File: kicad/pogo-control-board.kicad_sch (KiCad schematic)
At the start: 78 parts, among them CN1 CN_CTRL_1, CN2 CN_CTRL_2, CN3 CN_CTRL_3_PLACEHOLDER_TBD, J1 L IN, J10 BYPASS CV, J11 OFFSET CV, J12 BLEND CV, J13 FREQ CV1, J14 FB CV1, J15 DRIVE CV1, J16 FREQ CV2, J17 FB CV2, J18 DRIVE CV2, J19 FREQ CV3, J2 R IN, J20 FB CV3, J21 DRIVE CV3, J22 VCA CV IN, J23 LP1 CUT CV, J24 LP1 RES CV, J25 LP2 CUT CV, J26 LP2 RES CV, J27 HP CUT CV, J28 HP RES CV, J3 ENV L, J4 ENV R, J5 BAND OUT L, J6 BAND OUT R, J7 LEFT OUT, J8 RIGHT OUT, J9 MOD IN, SW1 GAIN 1x/5x, SW2 MOD SRC SEL, SW3 POLARITY, SW4 MODE

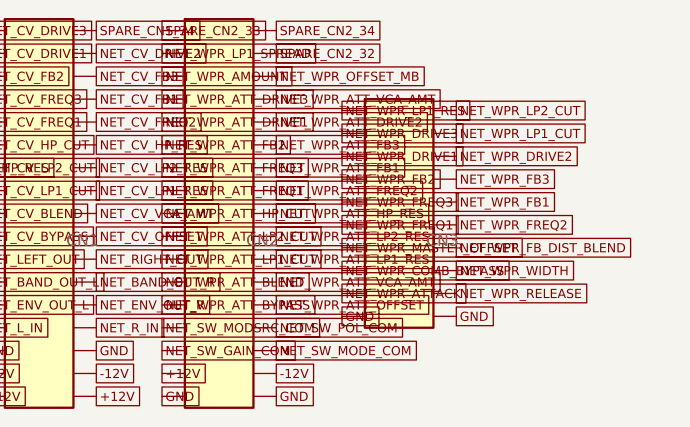
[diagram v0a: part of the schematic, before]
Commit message: Fix three net/connector bugs in KiCad control board generator
1. CN2 pin 28 duplicate: NET_WPR_ATT_VCA_AMT was assigned to both pin 12
   (attenuverter wiper, correct) and pin 28 (duplicate, wrong). Pin 28 is
   now SPARE_CN2_28. VCA AMT is destination #4 of 19 — it was already on pin 12.

2. CN3 overflow: extended from 20-pin to 24-pin (2×12). LP2_RES, HP_CUT, and
   HP_RES wipers were falling off the end of the 20-pin connector with only a
   comment. All 23 signals now fit with 1 spare.

3. MODE switch pins on CN2: pins 6–8 previously carried NET_SW_MODE_COM (the
   switch common — useless to the utility board). Now carry the 3 position
   outputs: NET_SW_MODE_SFT / _HRD / _WFD, which the utility board actually
   needs to decode CD4053 state. Added detailed comment on the 1-vs-3 switch
   ambiguity (panel-notes vs layout-notes conflict, unresolved, flagged).

Also updated kicad-process.md to reflect corrected CN3 size (24-pin), clarify
the layout-notes "19 + VCA AMT = 20" wording issue, and document MODE switch
encoding approach.

https://claude.ai/code/session_01JzWGptzLTqFkAZDHVU6Z8A
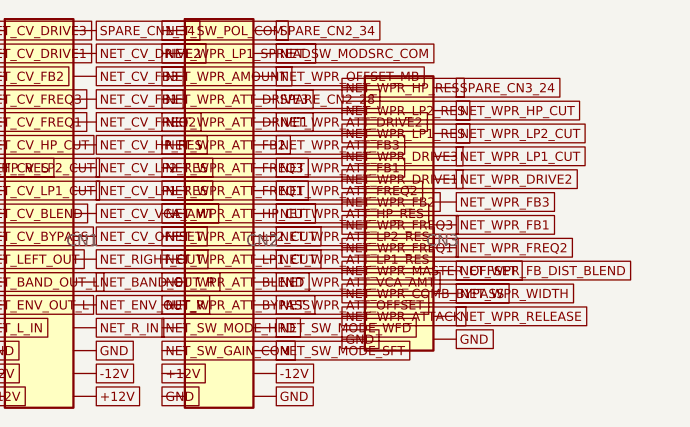
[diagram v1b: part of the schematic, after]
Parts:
- removed CN3: CN_CTRL_3_PLACEHOLDER_TBD, symbol Connector_IDC:IDC-Header_2x10_P2.54mm_Vertical
- added CN3: CN_CTRL_3_PLACEHOLDER_TBD, symbol Connector_IDC:IDC-Header_2x12_P2.54mm_Vertical
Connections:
- net SPARE_CN2_32 is gone; now on net NET_SW_MODSRC_COM: CN2.4 (Pin_4)
- net SPARE_CN2_33 is gone; now on net NET_SW_POL_COM: CN2.1 (Pin_1)
- net GND: now also CN3.23 (Pin_23), CN3.24 (Pin_24)
- net NET_SW_MODE_COM: no longer CN2.30 (Pin_30)
- net NET_SW_MODE_HRD: now also CN2.27 (Pin_27)
- net NET_SW_MODE_SFT: now also CN2.30 (Pin_30)
- net NET_SW_MODE_WFD: now also CN2.28 (Pin_28)
- net NET_SW_MODSRC_COM: no longer CN2.27 (Pin_27)
- net NET_SW_POL_COM: no longer CN2.28 (Pin_28)
- net NET_WPR_ATTACK: now also CN3.21 (Pin_21)
- net NET_WPR_ATT_VCA_AMT: no longer CN2.8 (Pin_8)
- net NET_WPR_COMB_BYPASS: now also CN3.19 (Pin_19)
- net NET_WPR_DRIVE1: now also CN3.9 (Pin_9)
- net NET_WPR_DRIVE2: now also CN3.10 (Pin_10)
- net NET_WPR_DRIVE3: now also CN3.7 (Pin_7)
- net NET_WPR_FB1: now also CN3.14 (Pin_14)
- net NET_WPR_FB2: now also CN3.11 (Pin_11)
- net NET_WPR_FB3: now also CN3.12 (Pin_12)
- net NET_WPR_FB_DIST_BLEND: now also CN3.18 (Pin_18)
- net NET_WPR_FREQ1: now also CN3.15 (Pin_15)
- net NET_WPR_FREQ2: now also CN3.16 (Pin_16)
- net NET_WPR_FREQ3: now also CN3.13 (Pin_13)
- net NET_WPR_HP_CUT: now also CN3.4 (Pin_4)
- net NET_WPR_HP_RES: now also CN3.1 (Pin_1)
- net NET_WPR_LP1_CUT: now also CN3.8 (Pin_8)
- net NET_WPR_LP1_RES: now also CN3.5 (Pin_5)
- net NET_WPR_LP2_CUT: now also CN3.6 (Pin_6)
- net NET_WPR_LP2_RES: now also CN3.3 (Pin_3)
- net NET_WPR_MASTER_OFFSET: now also CN3.17 (Pin_17)
- net NET_WPR_RELEASE: now also CN3.22 (Pin_22)
- net NET_WPR_WIDTH: now also CN3.20 (Pin_20)
- new net SPARE_CN2_28: CN2.8 (Pin_8)
- new net SPARE_CN3_24: CN3.2 (Pin_2)

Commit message: Fix control board schematic: expand CN2 to 40-pin, wire all switch nets
All switch commons now tie to +12V power symbols on the control board
(no orphan global labels). SP3T position outputs (MODE, MOD SRC, POLARITY)
each get 3 individual connector pins instead of sending the common pin:

CN_CTRL_2 expanded from 34-pin to 40-pin (2×20):
- Pins 32–34: MOD SRC L/MAX/AVG position outputs (SW2)
- Pins 35–37: POLARITY POS/OFF/NEG position outputs (SW3)
- Pin 38: ENV NORM return (utility board → MOD IN jack SW lug for normalling)

CN_CTRL_1 pin 34 changed from SPARE to NET_MOD_IN (MOD IN jack tip).

Result: zero problematic floating nets. Remaining 23 single-occurrence
nets are all intentional: 19 NET_MODBUS_NORM_* (CV override normalling,
documented in kicad-process.md), 4 SPARE_* connector spare pins.

Updated layout-notes.md and kicad-process.md to match.

https://claude.ai/code/session_01JzWGptzLTqFkAZDHVU6Z8A
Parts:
- removed CN2: CN_CTRL_2, symbol Connector_IDC:IDC-Header_2x17_P2.54mm_Vertical
- added CN2: CN_CTRL_2, symbol Connector_IDC:IDC-Header_2x20_P2.54mm_Vertical
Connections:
- net NET_SW_GAIN_1X is gone; now on net GND: SW1.2 (B)
- net NET_SW_GAIN_5X is gone; now on net +12V: SW1.1 (A)
- net NET_SW_MODE_COM is gone; now on net +12V: SW4.4 (C)
- net NET_SW_MODSRC_COM is gone; now on net +12V: SW2.4 (C)
- net NET_SW_POL_COM is gone; now on net +12V: SW3.4 (C)
- net SPARE_CN1_34 is gone; now on net NET_MOD_IN: CN1.2 (Pin_2)
- net +12V: now also CN2.37 (Pin_37)
- net -12V: now also CN2.38 (Pin_38)
- net GND: now also CN2.39 (Pin_39), CN2.40 (Pin_40)
- net NET_ENV_NORM: now also CN2.4 (Pin_4)
- net NET_SW_GAIN_COM: now also CN2.35 (Pin_35)
- net NET_SW_MODE_HRD: now also CN2.33 (Pin_33)
- net NET_SW_MODE_SFT: now also CN2.36 (Pin_36)
- net NET_SW_MODE_WFD: now also CN2.34 (Pin_34)
- net NET_SW_MODSRC_AVG: now also CN2.8 (Pin_8)
- net NET_SW_MODSRC_L: now also CN2.10 (Pin_10)
- net NET_SW_MODSRC_MAX: now also CN2.7 (Pin_7)
- net NET_SW_POL_NEG: now also CN2.3 (Pin_3)
- net NET_SW_POL_OFF: now also CN2.6 (Pin_6)
- net NET_SW_POL_POS: now also CN2.5 (Pin_5)
- net NET_WPR_AMOUNT: now also CN2.11 (Pin_11)
- net NET_WPR_ATT_BLEND: now also CN2.29 (Pin_29)
- net NET_WPR_ATT_BYPASS: now also CN2.31 (Pin_31)
- net NET_WPR_ATT_DRIVE1: now also CN2.15 (Pin_15)
- net NET_WPR_ATT_DRIVE2: now also CN2.16 (Pin_16)
- net NET_WPR_ATT_DRIVE3: now also CN2.13 (Pin_13)
- net NET_WPR_ATT_FB1: now also CN2.20 (Pin_20)
- net NET_WPR_ATT_FB2: now also CN2.17 (Pin_17)
- net NET_WPR_ATT_FB3: now also CN2.18 (Pin_18)
- net NET_WPR_ATT_FREQ1: now also CN2.21 (Pin_21)
- net NET_WPR_ATT_FREQ2: now also CN2.22 (Pin_22)
- net NET_WPR_ATT_FREQ3: now also CN2.19 (Pin_19)
- net NET_WPR_ATT_HP_CUT: now also CN2.23 (Pin_23)
- net NET_WPR_ATT_HP_RES: now also CN2.24 (Pin_24)
- net NET_WPR_ATT_LP1_CUT: now also CN2.27 (Pin_27)
- net NET_WPR_ATT_LP1_RES: now also CN2.28 (Pin_28)
- net NET_WPR_ATT_LP2_CUT: now also CN2.25 (Pin_25)
- net NET_WPR_ATT_LP2_RES: now also CN2.26 (Pin_26)
- net NET_WPR_ATT_OFFSET: now also CN2.32 (Pin_32)
- net NET_WPR_ATT_VCA_AMT: now also CN2.30 (Pin_30)
- net NET_WPR_LP1_SPREAD: now also CN2.9 (Pin_9)
- net NET_WPR_OFFSET_MB: now also CN2.12 (Pin_12)
- net SPARE_CN2_28: now also CN2.14 (Pin_14)
- new net SPARE_CN2_39: CN2.1 (Pin_1)
- new net SPARE_CN2_40: CN2.2 (Pin_2)
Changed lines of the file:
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@@
     (effects (font (size 1.016 1.016)) (justify left) (hide yes)))
 )
-(global_label "NET_SW_GAIN_1X"
-  (shape passive)
+(global_label "NET_SW_GAIN_COM"
+  (shape passive)
+  (at 63.810 50.000 0)
+  (effects (font (size 1.016 1.016)) (justify left))
+)
+(symbol
+  (lib_id "power:GND")
   (at 56.190 52.032 0)
-  (effects (font (size 1.016 1.016)) (justify left))
-)
-(global_label "NET_SW_GAIN_5X"
-  (shape passive)
+  (unit 1) (in_bom yes) (on_board yes)
+  (property "Reference" "#PWR" (at 56.190 50.032 0)
+    (effects (font (size 1.016 1.016)) (hide yes)))
+  (property "Value" "GND" (at 56.190 54.032 0)
+    (effects (font (size 1.016 1.016))))
+)
+(symbol
+  (lib_id "power:+12V")
   (at 56.190 47.968 0)
-  (effects (font (size 1.016 1.016)) (justify left))
-)
-(global_label "NET_SW_GAIN_COM"
-  (shape passive)
-  (at 63.810 50.000 0)
-  (effects (font (size 1.016 1.016)) (justify left))
+  (unit 1) (in_bom yes) (on_board yes)
+  (property "Reference" "#PWR" (at 56.190 45.968 0)
+    (effects (font (size 1.016 1.016)) (hide yes)))
+  (property "Value" "+12V" (at 56.190 49.968 0)
+    (effects (font (size 1.016 1.016))))
 )
 (symbol
@@
   (effects (font (size 1.016 1.016)) (justify left))
 )
-(global_label "NET_SW_MODSRC_COM"
-  (shape passive)
+(symbol
+  (lib_id "power:+12V")
   (at 83.810 50.000 0)
-  (effects (font (size 1.016 1.016)) (justify left))
+  (unit 1) (in_bom yes) (on_board yes)
+  (property "Reference" "#PWR" (at 83.810 48.000 0)
+    (effects (font (size 1.016 1.016)) (hide yes)))
+  (property "Value" "+12V" (at 83.810 52.000 0)
+    (effects (font (size 1.016 1.016))))
 )
 (symbol
@@
   (effects (font (size 1.016 1.016)) (justify left))
 )
-(global_label "NET_SW_POL_COM"
-  (shape passive)
+(symbol
+  (lib_id "power:+12V")
   (at 283.810 50.000 0)
-  (effects (font (size 1.016 1.016)) (justify left))
+  (unit 1) (in_bom yes) (on_board yes)
+  (property "Reference" "#PWR" (at 283.810 48.000 0)
+    (effects (font (size 1.016 1.016)) (hide yes)))
+  (property "Value" "+12V" (at 283.810 52.000 0)
+    (effects (font (size 1.016 1.016))))
 )
 (symbol
@@
   (effects (font (size 1.016 1.016)) (justify left))
 )
-(global_label "NET_SW_MODE_COM"
-  (shape passive)
+(symbol
+  (lib_id "power:+12V")
   (at 323.810 50.000 0)
-  (effects (font (size 1.016 1.016)) (justify left))
+  (unit 1) (in_bom yes) (on_board yes)
+  (property "Reference" "#PWR" (at 323.810 48.000 0)
+    (effects (font (size 1.016 1.016)) (hide yes)))
+  (property "Value" "+12V" (at 323.810 52.000 0)
+    (effects (font (size 1.016 1.016))))
 )
 (symbol
@@
   (effects (font (size 1.016 1.016)) (justify left))
 )
-(global_label "SPARE_CN1_34"
+(global_label "NET_MOD_IN"
   (shape passive)
   (at 1526.350 29.680 0)
@@
 )
 (symbol
-  (lib_id "Connector_IDC:IDC-Header_2x17_P2.54mm_Vertical")
+  (lib_id "Connector_IDC:IDC-Header_2x20_P2.54mm_Vertical")
   (at 1540.000 50.000 0)
   (unit 1)
@@
 (global_label "GND"
   (shape passive)
-  (at 1533.650 70.320 0)
-  (effects (font (size 1.016 1.016)) (justify left))
-)
-(global_label "GND"
-  (shape passive)
-  (at 1546.350 70.320 0)
-  (effects (font (size 1.016 1.016)) (justify left))
-)
-(global_label "+12V"
-  (shape passive)
-  (at 1533.650 67.780 0)
-  (effects (font (size 1.016 1.016)) (justify left))
-)
-(global_label "-12V"
-  (shape passive)
-  (at 1546.350 67.780 0)
+  (at 1533.650 74.130 0)
+  (effects (font (size 1.016 1.016)) (justify left))
+)
+(global_label "GND"
+  (shape passive)
+  (at 1546.350 74.130 0)
+  (effects (font (size 1.016 1.016)) (justify left))
+)
+(global_label "+12V"
+  (shape passive)
+  (at 1533.650 71.590 0)
+  (effects (font (size 1.016 1.016)) (justify left))
+)
+(global_label "-12V"
+  (shape passive)
+  (at 1546.350 71.590 0)
   (effects (font (size 1.016 1.016)) (justify left))
 )
 (global_label "NET_SW_GAIN_COM"
   (shape passive)
-  (at 1533.650 65.240 0)
+  (at 1533.650 69.050 0)
   (effects (font (size 1.016 1.016)) (justify left))
 )
 (global_label "NET_SW_MODE_SFT"
   (shape passive)
-  (at 1546.350 65.240 0)
+  (at 1546.350 69.050 0)
   (effects (font (size 1.016 1.016)) (justify left))
 )
 (global_label "NET_SW_MODE_HRD"
   (shape passive)
-  (at 1533.650 62.700 0)
+  (at 1533.650 66.510 0)
   (effects (font (size 1.016 1.016)) (justify left))
 )
 (global_label "NET_SW_MODE_WFD"
   (shape passive)
-  (at 1546.350 62.700 0)
+  (at 1546.350 66.510 0)
   (effects (font (size 1.016 1.016)) (justify left))
 )
 (global_label "NET_WPR_ATT_BYPASS"
   (shape passive)
-  (at 1533.650 60.160 0)
+  (at 1533.650 63.970 0)
   (effects (font (size 1.016 1.016)) (justify left))
 )
 (global_label "NET_WPR_ATT_OFFSET"
   (shape passive)
-  (at 1546.350 60.160 0)
+  (at 1546.350 63.970 0)
   (effects (font (size 1.016 1.016)) (justify left))
 )
 (global_label "NET_WPR_ATT_BLEND"
   (shape passive)
-  (at 1533.650 57.620 0)
+  (at 1533.650 61.430 0)
   (effects (font (size 1.016 1.016)) (justify left))
 )
 (global_label "NET_WPR_ATT_VCA_AMT"
   (shape passive)
-  (at 1546.350 57.620 0)
+  (at 1546.350 61.430 0)
   (effects (font (size 1.016 1.016)) (justify left))
 )
 (global_label "NET_WPR_ATT_LP1_CUT"
   (shape passive)
-  (at 1533.650 55.080 0)
+  (at 1533.650 58.890 0)
   (effects (font (size 1.016 1.016)) (justify left))
 )
 (global_label "NET_WPR_ATT_LP1_RES"
   (shape passive)
-  (at 1546.350 55.080 0)
+  (at 1546.350 58.890 0)
   (effects (font (size 1.016 1.016)) (justify left))
 )
 (global_label "NET_WPR_ATT_LP2_CUT"
   (shape passive)
-  (at 1533.650 52.540 0)
+  (at 1533.650 56.350 0)
   (effects (font (size 1.016 1.016)) (justify left))
 )
 (global_label "NET_WPR_ATT_LP2_RES"
   (shape passive)
-  (at 1546.350 52.540 0)
+  (at 1546.350 56.350 0)
   (effects (font (size 1.016 1.016)) (justify left))
 )
 (global_label "NET_WPR_ATT_HP_CUT"
   (shape passive)
-  (at 1533.650 50.000 0)
+  (at 1533.650 53.810 0)
   (effects (font (size 1.016 1.016)) (justify left))
 )
 (global_label "NET_WPR_ATT_HP_RES"
   (shape passive)
-  (at 1546.350 50.000 0)
+  (at 1546.350 53.810 0)
   (effects (font (size 1.016 1.016)) (justify left))
 )
 (global_label "NET_WPR_ATT_FREQ1"
   (shape passive)
-  (at 1533.650 47.460 0)
+  (at 1533.650 51.270 0)
   (effects (font (size 1.016 1.016)) (justify left))
 )
 (global_label "NET_WPR_ATT_FREQ2"
   (shape passive)
-  (at 1546.350 47.460 0)
+  (at 1546.350 51.270 0)
   (effects (font (size 1.016 1.016)) (justify left))
 )
 (global_label "NET_WPR_ATT_FREQ3"
   (shape passive)
-  (at 1533.650 44.920 0)
+  (at 1533.650 48.730 0)
   (effects (font (size 1.016 1.016)) (justify left))
 )
 (global_label "NET_WPR_ATT_FB1"
   (shape passive)
-  (at 1546.350 44.920 0)
+  (at 1546.350 48.730 0)
   (effects (font (size 1.016 1.016)) (justify left))
 )
 (global_label "NET_WPR_ATT_FB2"
   (shape passive)
-  (at 1533.650 42.380 0)
+  (at 1533.650 46.190 0)
   (effects (font (size 1.016 1.016)) (justify left))
 )
 (global_label "NET_WPR_ATT_FB3"
   (shape passive)
-  (at 1546.350 42.380 0)
+  (at 1546.350 46.190 0)
   (effects (font (size 1.016 1.016)) (justify left))
 )
 (global_label "NET_WPR_ATT_DRIVE1"
   (shape passive)
-  (at 1533.650 39.840 0)
+  (at 1533.650 43.650 0)
   (effects (font (size 1.016 1.016)) (justify left))
 )
 (global_label "NET_WPR_ATT_DRIVE2"
   (shape passive)
-  (at 1546.350 39.840 0)
+  (at 1546.350 43.650 0)
   (effects (font (size 1.016 1.016)) (justify left))
 )
 (global_label "NET_WPR_ATT_DRIVE3"
   (shape passive)
-  (at 1533.650 37.300 0)
+  (at 1533.650 41.110 0)
   (effects (font (size 1.016 1.016)) (justify left))
 )
 (global_label "SPARE_CN2_28"
   (shape passive)
-  (at 1546.350 37.300 0)
+  (at 1546.350 41.110 0)
   (effects (font (size 1.016 1.016)) (justify left))
 )
 (global_label "NET_WPR_AMOUNT"
   (shape passive)
-  (at 1533.650 34.760 0)
+  (at 1533.650 38.570 0)
   (effects (font (size 1.016 1.016)) (justify left))
 )
 (global_label "NET_WPR_OFFSET_MB"
   (shape passive)
-  (at 1546.350 34.760 0)
+  (at 1546.350 38.570 0)
   (effects (font (size 1.016 1.016)) (justify left))
 )
 (global_label "NET_WPR_LP1_SPREAD"
   (shape passive)
-  (at 1533.650 32.220 0)
-  (effects (font (size 1.016 1.016)) (justify left))
-)
-(global_label "NET_SW_MODSRC_COM"
-  (shape passive)
-  (at 1546.350 32.220 0)
-  (effects (font (size 1.016 1.016)) (justify left))
-)
-(global_label "NET_SW_POL_COM"
-  (shape passive)
-  (at 1533.650 29.680 0)
-  (effects (font (size 1.016 1.016)) (justify left))
-)
-(global_label "SPARE_CN2_34"
-  (shape passive)
-  (at 1546.350 29.680 0)
-  (effects (font (size 1.016 1.016)) (justify left))
-)
+  (at 1533.650 36.030 0)
+  (effects (font (size 1.016 1.016)) (justify left))
+)
+(global_label "NET_SW_MODSRC_L"
+  (shape passive)
+  (at 1546.350 36.030 0)
+  (effects (font (size 1.016 1.016)) (justify left))
+)
+(global_label "NET_SW_MODSRC_MAX"
+  (shape passive)
+  (at 1533.650 33.490 0)
+  (effects (font (size 1.016 1.016)) (justify left))
+)
+(global_label "NET_SW_MODSRC_AVG"
+  (shape passive)
+  (at 1546.350 33.490 0)
+  (effects (font (size 1.016 1.016)) (justify left))
+)
+(global_label "NET_SW_POL_POS"
+  (shape passive)
+  (at 1533.650 30.950 0)
+  (effects (font (size 1.016 1.016)) (justify left))
+)
+(global_label "NET_SW_POL_OFF"
+  (shape passive)
+  (at 1546.350 30.950 0)
+  (effects (font (size 1.016 1.016)) (justify left))
+)
+(global_label "NET_SW_POL_NEG"
+  (shape passive)
+  (at 1533.650 28.410 0)
+  (effects (font (size 1.016 1.016)) (justify left))
+)
+(global_label "NET_ENV_NORM"
+  (shape passive)
+  (at 1546.350 28.410 0)
+  (effects (font (size 1.016 1.016)) (justify left))
+)
+(global_label "SPARE_CN2_39"
+  (shape passive)
+  (at 1533.650 25.870 0)
+  (effects (font (size 1.016 1.016)) (justify left))
+)
+(global_label "SPARE_CN2_40"
+  (shape passive)
+  (at 1546.350 25.870 0)
+  (effects (font (size 1.016 1.016)) (justify left))
+)

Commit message: Collapse 19 MODBUS_NORM_* nets into single NET_MODBUS_NORM (1 connector pin)
All 19 CV override jack SW lugs now share one net (NET_MODBUS_NORM) wired
together on the control board PCB. The utility board drives CN_CTRL_2 pin 39
with the processed Mod Bus output (post-AMOUNT/OFFSET, buffered). When no
cable is plugged into any CV override jack, its Thonkiconn switch connects
tip to SW, so the attenuverter input sees the Mod Bus.

This saves 18 connector pins vs. individual normalling signals and eliminates
all 19 previously-floating NET_MODBUS_NORM_* labels.

Result: only 3 single-occurrence nets remain — all are intentional spare pins
(SPARE_CN2_28, SPARE_CN2_40, SPARE_CN3_24).

Updated layout-notes.md and kicad-process.md to document the design.

https://claude.ai/code/session_01JzWGptzLTqFkAZDHVU6Z8A
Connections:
- net SPARE_CN2_39 renamed NET_MODBUS_NORM
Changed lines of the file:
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@@
   (effects (font (size 1.016 1.016)) (justify left))
 )
-(global_label "NET_MODBUS_NORM_BYPASS"
+(global_label "NET_MODBUS_NORM"
   (shape passive)
   (at 360.000 44.920 0)
@@
   (effects (font (size 1.016 1.016)) (justify left))
 )
-(global_label "NET_MODBUS_NORM_OFFSET"
+(global_label "NET_MODBUS_NORM"
   (shape passive)
   (at 380.000 44.920 0)
@@
   (effects (font (size 1.016 1.016)) (justify left))
 )
-(global_label "NET_MODBUS_NORM_BLEND"
+(global_label "NET_MODBUS_NORM"
   (shape passive)
   (at 400.000 44.920 0)
@@
   (effects (font (size 1.016 1.016)) (justify left))
 )
-(global_label "NET_MODBUS_NORM_FREQ1"
+(global_label "NET_MODBUS_NORM"
   (shape passive)
   (at 600.000 44.920 0)
@@
   (effects (font (size 1.016 1.016)) (justify left))
 )
-(global_label "NET_MODBUS_NORM_FB1"
+(global_label "NET_MODBUS_NORM"
   (shape passive)
   (at 620.000 44.920 0)
@@
   (effects (font (size 1.016 1.016)) (justify left))
 )
-(global_label "NET_MODBUS_NORM_DRIVE1"
+(global_label "NET_MODBUS_NORM"
   (shape passive)
   (at 640.000 44.920 0)
@@
   (effects (font (size 1.016 1.016)) (justify left))
 )
-(global_label "NET_MODBUS_NORM_FREQ2"
+(global_label "NET_MODBUS_NORM"
   (shape passive)
   (at 780.000 44.920 0)
@@
   (effects (font (size 1.016 1.016)) (justify left))
 )
-(global_label "NET_MODBUS_NORM_FB2"
+(global_label "NET_MODBUS_NORM"
   (shape passive)
   (at 800.000 44.920 0)
@@
   (effects (font (size 1.016 1.016)) (justify left))
 )
-(global_label "NET_MODBUS_NORM_DRIVE2"
+(global_label "NET_MODBUS_NORM"
   (shape passive)
   (at 820.000 44.920 0)
@@
   (effects (font (size 1.016 1.016)) (justify left))
 )
-(global_label "NET_MODBUS_NORM_FREQ3"
+(global_label "NET_MODBUS_NORM"
   (shape passive)
   (at 960.000 44.920 0)
@@
   (effects (font (size 1.016 1.016)) (justify left))
 )
-(global_label "NET_MODBUS_NORM_FB3"
+(global_label "NET_MODBUS_NORM"
   (shape passive)
   (at 980.000 44.920 0)
@@
   (effects (font (size 1.016 1.016)) (justify left))
 )
-(global_label "NET_MODBUS_NORM_DRIVE3"
+(global_label "NET_MODBUS_NORM"
   (shape passive)
   (at 1000.000 44.920 0)
@@
   (effects (font (size 1.016 1.016)) (justify left))
 )
-(global_label "NET_MODBUS_NORM_VCA_AMT"
+(global_label "NET_MODBUS_NORM"
   (shape passive)
   (at 1040.000 44.920 0)
@@
   (effects (font (size 1.016 1.016)) (justify left))
 )
-(global_label "NET_MODBUS_NORM_LP1_CUT"
+(global_label "NET_MODBUS_NORM"
   (shape passive)
   (at 1160.000 44.920 0)
@@
   (effects (font (size 1.016 1.016)) (justify left))
 )
-(global_label "NET_MODBUS_NORM_LP1_RES"
+(global_label "NET_MODBUS_NORM"
   (shape passive)
   (at 1180.000 44.920 0)
@@
   (effects (font (size 1.016 1.016)) (justify left))
 )
-(global_label "NET_MODBUS_NORM_LP2_CUT"
+(global_label "NET_MODBUS_NORM"
   (shape passive)
   (at 1320.000 44.920 0)
@@
   (effects (font (size 1.016 1.016)) (justify left))
 )
-(global_label "NET_MODBUS_NORM_LP2_RES"
+(global_label "NET_MODBUS_NORM"
   (shape passive)
   (at 1340.000 44.920 0)
@@
   (effects (font (size 1.016 1.016)) (justify left))
 )
-(global_label "NET_MODBUS_NORM_HP_CUT"
+(global_label "NET_MODBUS_NORM"
   (shape passive)
   (at 1480.000 44.920 0)
@@
   (effects (font (size 1.016 1.016)) (justify left))
 )
-(global_label "NET_MODBUS_NORM_HP_RES"
+(global_label "NET_MODBUS_NORM"
   (shape passive)
   (at 1500.000 44.920 0)
@@
   (effects (font (size 1.016 1.016)) (justify left))
 )
-(global_label "SPARE_CN2_39"
+(global_label "NET_MODBUS_NORM"
   (shape passive)
   (at 1533.650 25.870 0)
